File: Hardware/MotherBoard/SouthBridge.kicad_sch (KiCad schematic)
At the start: 14 parts, among them J12 NMI_PULLUP, J14 IRQ0_PULLUP, J3 ISA00, J4 ISA10, J7 ISA01, J8 ISA11, U10 74HC245, U11 74HC245, U12 74HC245, U13 74HC541, U14 74HC541, U9 74HC245

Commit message: Fix
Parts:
- removed J3: ISA00, Connector_PinSocket_2.54mm:PinSocket_1x16_P2.54mm_Vertical, symbol Connector:Conn_01x16_Female
- removed J4: ISA10, Connector_PinSocket_2.54mm:PinSocket_1x16_P2.54mm_Vertical, symbol Connector:Conn_01x16_Female
- removed J7: ISA01, Connector_PinSocket_2.54mm:PinSocket_1x16_P2.54mm_Vertical, symbol Connector:Conn_01x16_Female
- removed J8: ISA11, Connector_PinSocket_2.54mm:PinSocket_1x16_P2.54mm_Vertical, symbol Connector:Conn_01x16_Female
- added J3: ISA1, Connector_PinSocket_2.54mm:PinSocket_2x16_P2.54mm_Vertical, symbol Connector_TheRLab:Conn_02x16_Female_2units
- added J4: ISA0, Connector_PinSocket_2.54mm:PinSocket_2x16_P2.54mm_Vertical, symbol Connector_TheRLab:Conn_02x16_Female_2units
- R1, R6: value 10K -> 3K3
- U10, U11, U12, U9: footprint digikey-footprints:DIP-20_W7.62mm -> Package_DIP:DIP-20_W7.62mm
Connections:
- net +5V: now also J4.16 (Pin_16); no longer U10.20 (VCC), U11.20 (VCC), U9.20 (VCC)
- net CLOCK: now also J3.12 (Pin_12), J4.12 (Pin_12)
- net DMAB: now also J3.15 (Pin_15)
- net GND: now also J3.13 (Pin_13), J4.13 (Pin_13), J4.15 (Pin_15)
- net IRQ0B: now also J4.11 (Pin_11)
- net NMIB: now also J3.11 (Pin_11)
- net PORT1B: now also J4.10 (Pin_10)
- net PORT2B: now also J3.10 (Pin_10)
- net RESET: now also J3.14 (Pin_14), J4.14 (Pin_14)
- net RW: now also J3.9 (Pin_9), J4.9 (Pin_9); no longer U11.1 (DIR)
- net at U9.18 (B1): now also J3.17 (Pin_17)
- net at U10.17 (B2): now also J3.26 (Pin_26)
- net at U10.16 (B3): now also J3.27 (Pin_27)
- net at U10.15 (B4): now also J3.28 (Pin_28)
- net at U10.14 (B5): now also J3.29 (Pin_29)
- net at U10.13 (B6): now also J3.30 (Pin_30)
- net at U10.12 (B7): now also J3.31 (Pin_31)
- net at U10.11 (B8): now also J3.32 (Pin_32)
- net at U9.17 (B2): now also J3.18 (Pin_18)
- net at U9.16 (B3): now also J3.19 (Pin_19)
- net at U9.15 (B4): now also J3.20 (Pin_20)
- net at U9.14 (B5): now also J3.21 (Pin_21)
- net at U9.13 (B6): now also J3.22 (Pin_22)
- net at U9.12 (B7): now also J3.23 (Pin_23)
- net at U9.11 (B8): now also J3.24 (Pin_24)
- net at U10.18 (B1): now also J3.25 (Pin_25)
- net at U13.11 (Y7): now also J4.32 (Pin_32)
- net at U13.12 (Y6): now also J4.31 (Pin_31)
- net at U13.13 (Y5): now also J4.30 (Pin_30)
- net at U13.14 (Y4): now also J4.29 (Pin_29)
- net at U13.15 (Y3): now also J4.28 (Pin_28)
- net at U13.16 (Y2): now also J4.27 (Pin_27)
- net at U13.17 (Y1): now also J4.26 (Pin_26)
- net at U13.18 (Y0): now also J4.25 (Pin_25)
- net at U12.2 (A1): now also J4.1 (Pin_1)
- net at U12.3 (A2): now also J4.2 (Pin_2)
- net at U12.4 (A3): now also J4.3 (Pin_3)
- net at U12.5 (A4): now also J4.4 (Pin_4)
- net at U12.6 (A5): now also J4.5 (Pin_5)
- net at U12.7 (A6): now also J4.6 (Pin_6)
- net at U12.8 (A7): now also J4.7 (Pin_7)
- net at U12.9 (A8): now also J4.8 (Pin_8)
- net at U14.11 (Y7): now also J4.24 (Pin_24)
- net at U14.12 (Y6): now also J4.23 (Pin_23)
- net at U14.13 (Y5): now also J4.22 (Pin_22)
- net at U14.14 (Y4): now also J4.21 (Pin_21)
- net at U14.15 (Y3): now also J4.20 (Pin_20)
- net at U14.16 (Y2): now also J4.19 (Pin_19)
- net at U14.17 (Y1): now also J4.18 (Pin_18)
- net at U14.18 (Y0): now also J4.17 (Pin_17)
- net at U11.2 (A1): now also J3.1 (Pin_1)
- net at U11.3 (A2): now also J3.2 (Pin_2)
- net at U11.4 (A3): now also J3.3 (Pin_3)
- net at U11.5 (A4): now also J3.4 (Pin_4)
- net at U11.6 (A5): now also J3.5 (Pin_5)
- net at U11.7 (A6): now also J3.6 (Pin_6)
- net at U11.8 (A7): now also J3.7 (Pin_7)
- net at U11.9 (A8): now also J3.8 (Pin_8)
- new net DMARW: U11.1 (DIR)
- new net VCC: J3.16 (Pin_16), U10.20 (VCC), U11.20 (VCC), U9.20 (VCC)
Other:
- note added: "Address Bus 2 (with DMA)"
- note added: "Data Bus 1"
- note added: "Data Bus 2 (with DMA)"
- note removed: "Address Bus 2"
- note removed: "Data Bus 1 (with DMA)"
- note removed: "Data Bus 2"
- company: (none) -> Romuald Rousseau
- title: (none) -> Miniish
- moved on the sheet: J12, J14, R1, R6, U11, U12

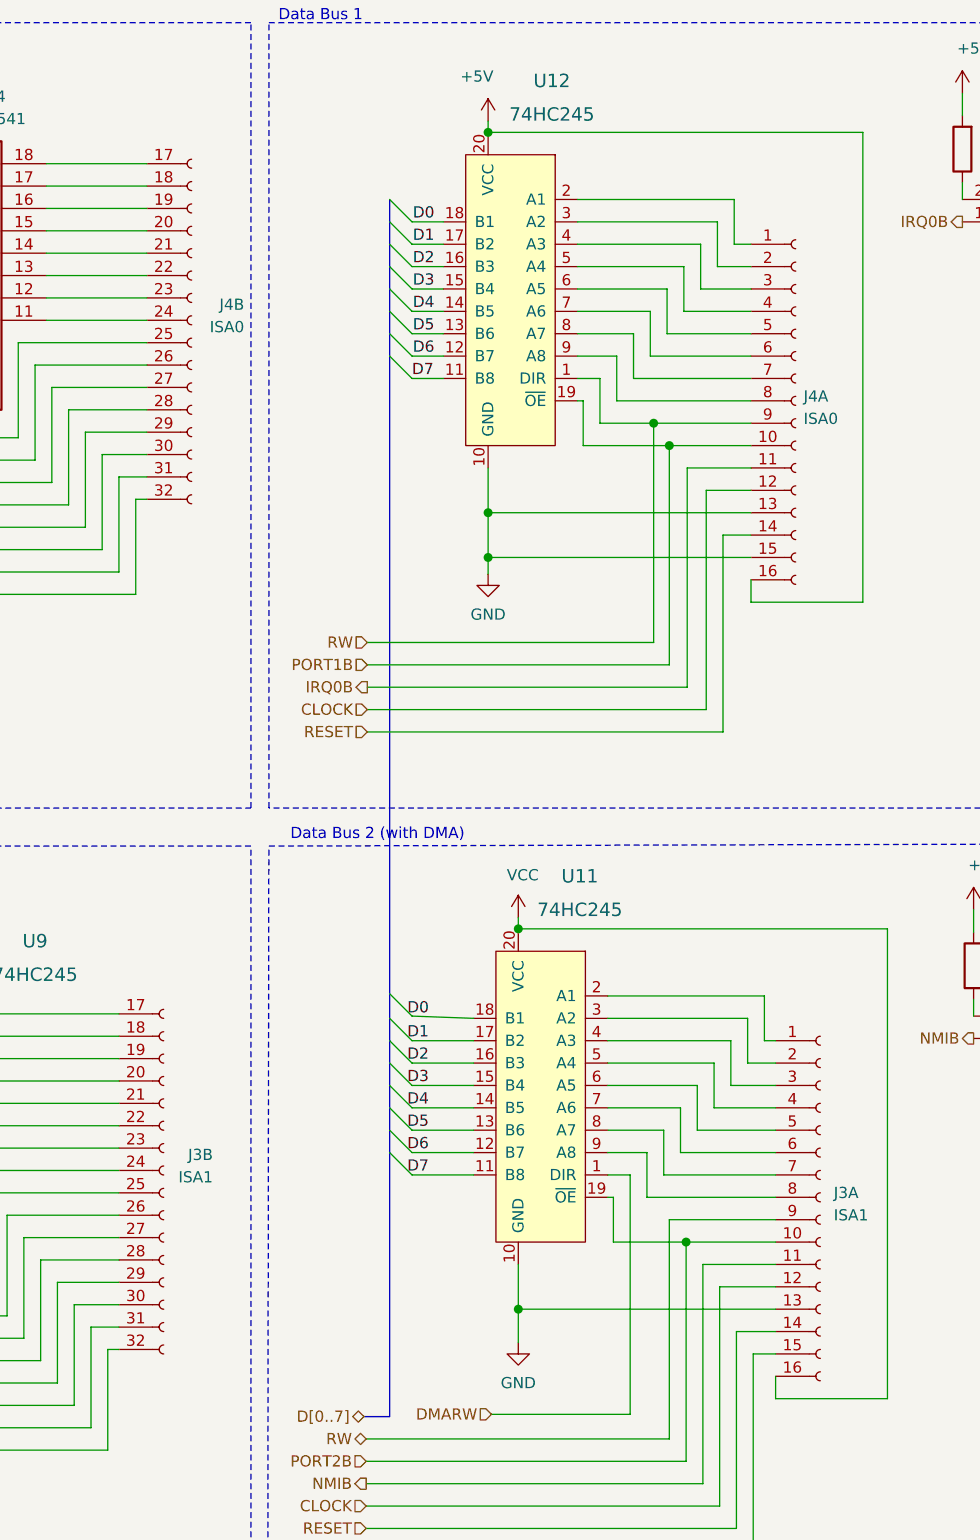
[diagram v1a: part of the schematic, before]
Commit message: Update to Kicad 6.0
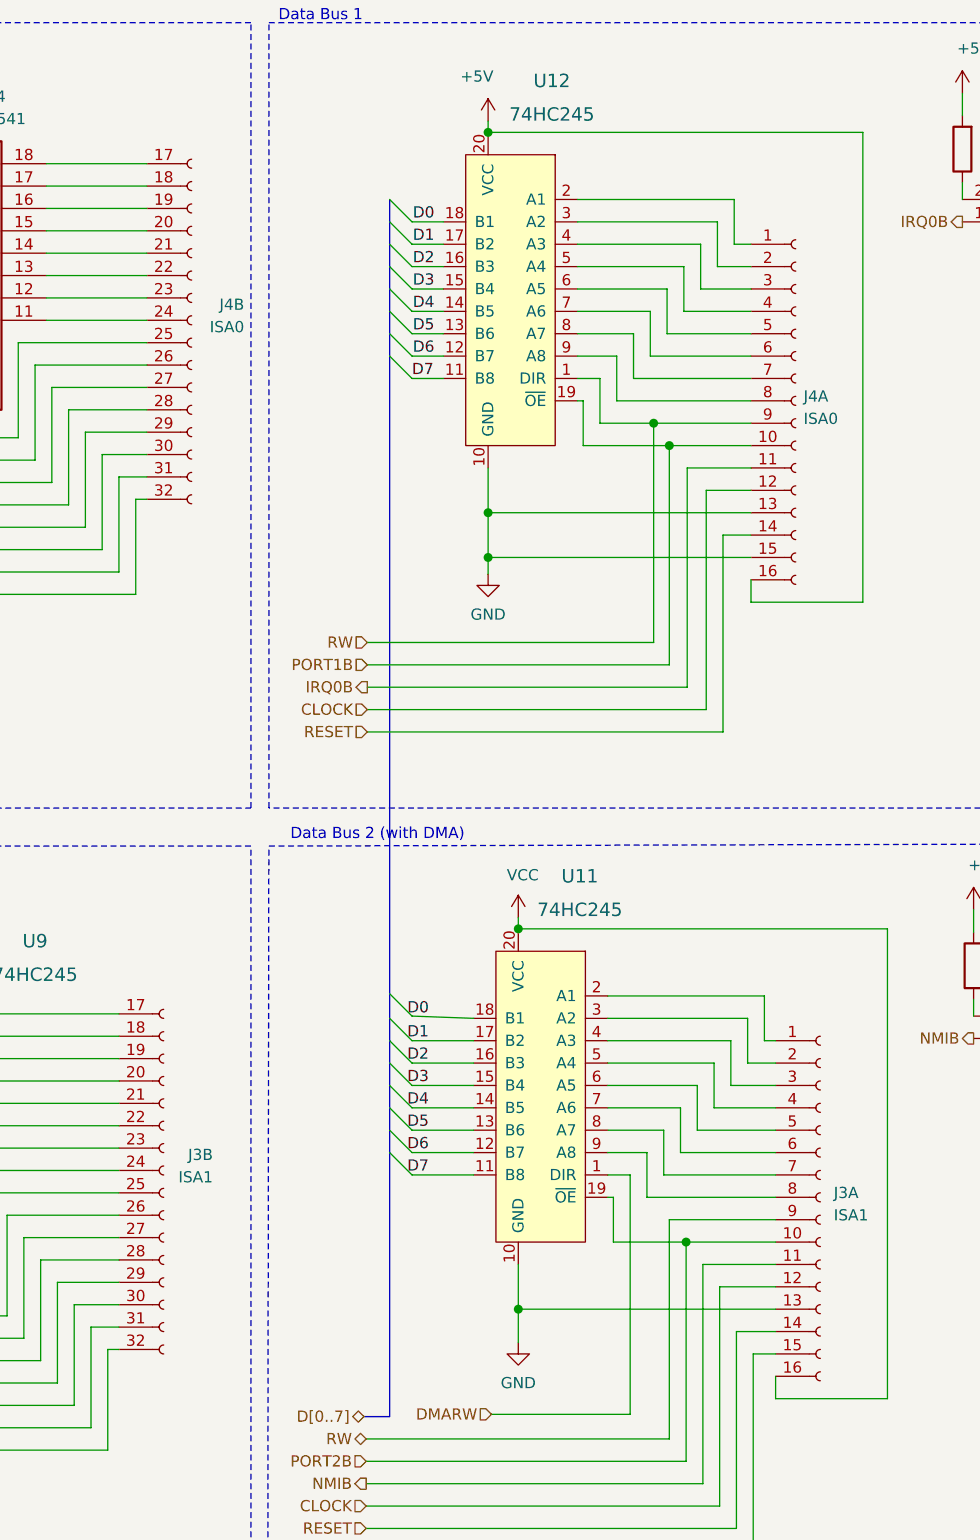
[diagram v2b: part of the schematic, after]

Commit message: New motherboard version
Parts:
- removed J12: NMI_PULLUP, Connector_PinHeader_2.54mm:PinHeader_1x02_P2.54mm_Vertical, symbol Connector:Conn_01x02_Male
- removed J14: IRQ0_PULLUP, Connector_PinHeader_2.54mm:PinHeader_1x02_P2.54mm_Vertical, symbol Connector:Conn_01x02_Male
- removed J3: ISA1, Connector_PinSocket_2.54mm:PinSocket_2x16_P2.54mm_Vertical, symbol Connector_TheRLab:Conn_02x16_Female_2units
- removed J4: ISA0, Connector_PinSocket_2.54mm:PinSocket_2x16_P2.54mm_Vertical, symbol Connector_TheRLab:Conn_02x16_Female_2units
- removed R1: 3K3, Resistor_THT:R_Axial_DIN0207_L6.3mm_D2.5mm_P10.16mm_Horizontal, symbol Device:R
- removed U10, U11, U12, U9: 74HC245, Package_DIP:DIP-20_W7.62mm, symbol dk_Logic-Buffers-Drivers-Receivers-Transceivers:SN74LVC245AN
- removed U13, U14: 74HC541, Package_DIP:DIP-20_W7.62mm, symbol 74xx:74HCT541
- added C4 (x2): 100nF, Capacitor_THT:C_Disc_D5.0mm_W2.5mm_P2.50mm, symbol Device:C_Small
- added C8: 220nF, Capacitor_THT:C_Disc_D5.0mm_W2.5mm_P5.00mm, symbol Device:C_Small
- added J14: IRQ2_PULLUP, Connector_PinHeader_2.54mm:PinHeader_1x02_P2.54mm_Vertical, symbol Connector:Conn_01x02_Pin
- added J15: IRQ5_PULLUP, Connector_PinHeader_2.54mm:PinHeader_1x02_P2.54mm_Vertical, symbol Connector:Conn_01x02_Pin
- added J15: IRQ4_PULLUP, Connector_PinHeader_2.54mm:PinHeader_1x02_P2.54mm_Vertical, symbol Connector:Conn_01x02_Pin
- added J15: IRQ3_PULLUP, Connector_PinHeader_2.54mm:PinHeader_1x02_P2.54mm_Vertical, symbol Connector:Conn_01x02_Pin
- added J15: IRQ6_PULLUP, Connector_PinHeader_2.54mm:PinHeader_1x02_P2.54mm_Vertical, symbol Connector:Conn_01x02_Pin
- added R7 (x4): 3K3, Resistor_THT:R_Axial_DIN0207_L6.3mm_D2.5mm_P10.16mm_Horizontal, symbol Device:R
- added U5: 74HC148, Package_DIP:DIP-16_W7.62mm, symbol 74xx:74LS148
- added U6: 74HC574, Package_DIP:DIP-20_W7.62mm, symbol 74xx:74HCT574
- added U7: ATF22V10B, Package_DIP:DIP-24_W7.62mm, symbol Logic_Programmable:PAL20RS10
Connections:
- net +5V: now also C4.1, C4.1, C8.1, R7.2, R7.2, R7.2, R7.2, U5.10 (IO), U5.16 (VCC), U6.20 (VCC), U7.24 (VCC)
- net A10: now also U7.7 (I5)
- net A11: now also U7.6 (I4)
- net A12: now also U7.5 (I3)
- net A13: now also U7.4 (I2)
- net A14: now also U7.3 (I1)
- net A15: now also U7.2 (I0)
- net A8: now also U7.9 (I7)
- net A9: now also U7.8 (I6)
- net CLOCK: now also U6.11 (Cp), U7.1 (CLK)
- net D0: now also U6.19 (Q0)
- net D1: now also U6.18 (Q1)
- net D2: now also U6.17 (Q2)
- net D3: now also U6.16 (Q3)
- net D4: now also U6.15 (Q4)
- net D5: now also U6.14 (Q5)
- net D6: now also U6.13 (Q6)
- net D7: now also U6.12 (Q7)
- net DMAB: now also U7.10 (I8)
- net GND: now also C4.2, C4.2, C8.2, U5.5 (EI), U5.8 (GND), U6.10 (GND), U6.2 (D0), U6.6 (D4), U6.7 (D5), U6.8 (D6), U6.9 (D7), U7.11 (I9), U7.12 (GND), U7.13 (~{OE})
- net IRQ0B: now also U5.4 (I7)
- net at R6.1: now also J14.2 (Pin_2)
- new net: J15.2 (Pin_2), R7.1 (x4)
- new net: U5.6 (S2), U6.5 (D3)
- new net: U5.7 (S1), U6.4 (D2)
- new net: U5.9 (S0), U6.3 (D1)
- new net: U6.1 (OE), U7.23 (O0)
- new net CIA1CSB: U7.20 (O3)
- new net CIA2CSB: U7.21 (O2)
- new net IRQ1B: U5.3 (I6)
- new net IRQ2B: J14.1 (Pin_1), U5.2 (I5)
- new net IRQ3B: J15.1 (Pin_1), U5.1 (I4)
- new net IRQ4B: J15.1 (Pin_1), U5.13 (I3)
- new net IRQ5B: J15.1 (Pin_1), U5.12 (I2)
- new net IRQ6B: J15.1 (Pin_1), U5.11 (I1)
- new net IRQB: U5.14 (GS)
- new net PORT1CSB: U7.17 (O6)
- new net PORT2CSB: U7.18 (O5)
- new net PORT3CSB: U7.19 (O4)
- new net RAMCSB: U7.15 (O8)
- new net ROMCSB: U7.16 (O7)
- new net USRCSB: U7.22 (O1)
- no-connect marks 0 -> 2
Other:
- note added: "Controller Hub"
- note added: "Decoder IRQ"
- note added: "Decouplings and Pullups"
- note removed: "Address Bus 1"
- note removed: "Address Bus 2 (with DMA)"
- note removed: "Data Bus 1"
- note removed: "Data Bus 2 (with DMA)"

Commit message: A lot of new hardware
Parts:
- C8: footprint Capacitor_THT:C_Disc_D5.0mm_W2.5mm_P5.00mm -> Capacitor_THT:C_Disc_D5.0mm_W2.5mm_P2.50mm
- J14: value IRQ2_PULLUP -> IRQ2
- J15: value IRQ5_PULLUP -> IRQ5
- J15: value IRQ4_PULLUP -> IRQ4
- J15: value IRQ3_PULLUP -> IRQ3
- J15: value IRQ6_PULLUP -> IRQ6
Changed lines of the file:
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@@
       (effects (font (size 1.27 1.27)) (justify left))
     )
-    (property "Footprint" "Capacitor_THT:C_Disc_D5.0mm_W2.5mm_P5.00mm" (at 215.9 67.31 0)
+    (property "Footprint" "Capacitor_THT:C_Disc_D5.0mm_W2.5mm_P2.50mm" (at 215.9 67.31 0)
       (effects (font (size 1.27 1.27)) hide)
     )
@@
       (effects (font (size 1.27 1.27)) (justify right))
     )
-    (property "Value" "IRQ5_PULLUP" (at 260.35 102.235 0)
+    (property "Value" "IRQ5" (at 260.35 102.235 0)
       (effects (font (size 1.27 1.27)) (justify right))
     )
@@
       (effects (font (size 1.27 1.27)) (justify right))
     )
-    (property "Value" "IRQ4_PULLUP" (at 260.35 131.445 0)
+    (property "Value" "IRQ4" (at 260.35 131.445 0)
       (effects (font (size 1.27 1.27)) (justify right))
     )
@@
       (effects (font (size 1.27 1.27)) (justify right))
     )
-    (property "Value" "IRQ2_PULLUP" (at 229.87 102.235 0)
+    (property "Value" "IRQ2" (at 229.87 102.235 0)
       (effects (font (size 1.27 1.27)) (justify right))
     )
@@
       (effects (font (size 1.27 1.27)) (justify right))
     )
-    (property "Value" "IRQ3_PULLUP" (at 229.87 131.445 0)
+    (property "Value" "IRQ3" (at 229.87 131.445 0)
       (effects (font (size 1.27 1.27)) (justify right))
     )
@@
       (effects (font (size 1.27 1.27)) (justify right))
     )
-    (property "Value" "IRQ6_PULLUP" (at 259.08 75.565 0)
-      (effects (font (size 1.27 1.27)) (justify right))
-    )
+    (property "Value" "IRQ6" (at 259.08 75.565 0)
+      (effects (font (size 1.27 1.27)) (justify right))
+    )

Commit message: Add ArduinoMultiInterface
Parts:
- renumbered C4 to C10, C4 to C9, J15 to J10, J15 to J11, J14 to J7, J15 to J8, J15 to J9, R7 to R10, R7 to R8, R7 to R9
